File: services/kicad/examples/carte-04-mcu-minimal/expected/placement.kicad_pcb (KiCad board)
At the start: 2 copper layers, 60 x 45 mm, 15 parts, among them J1 IN_5V, J2 SWD, U1 STM32F103C8T6, U2 AMS1117-3.3

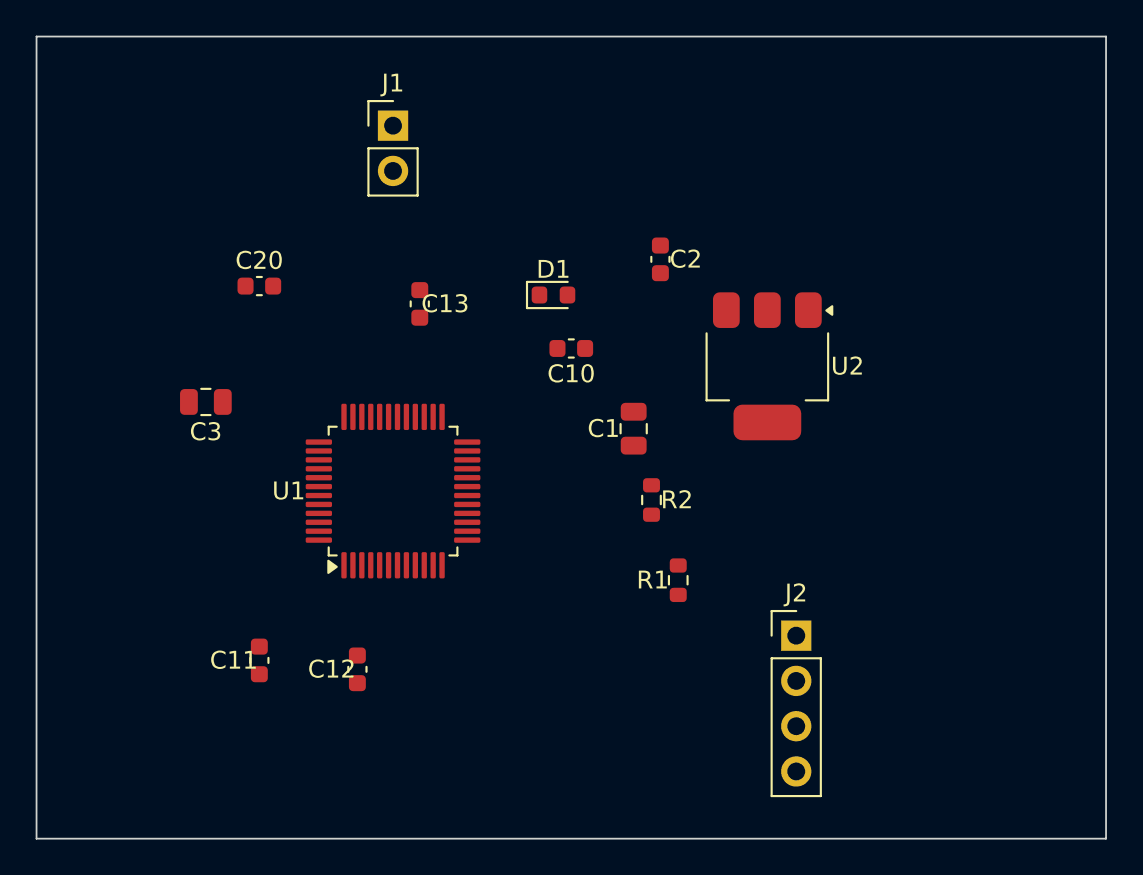
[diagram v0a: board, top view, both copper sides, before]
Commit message: examples: carte-01 a 07 -- placement valide et gele (phase 1) puis route dessus (phase 2) : 100 %, 0 erreur, 2 couches
Sequence en deux phases demandee par l'utilisateur : valider_placements.py (critere pro : chaque broche VDD a sa capa a <= 3,5 mm) puis banc_exemples.py --placement-fige. 30 s a 2,6 min de routage par carte.

Co-Authored-By: Claude Fable 5.1 <noreply@anthropic.com>

Claude-Session: https://claude.ai/code/session_01TnMqm4La2CxQHHB5K8aSSV
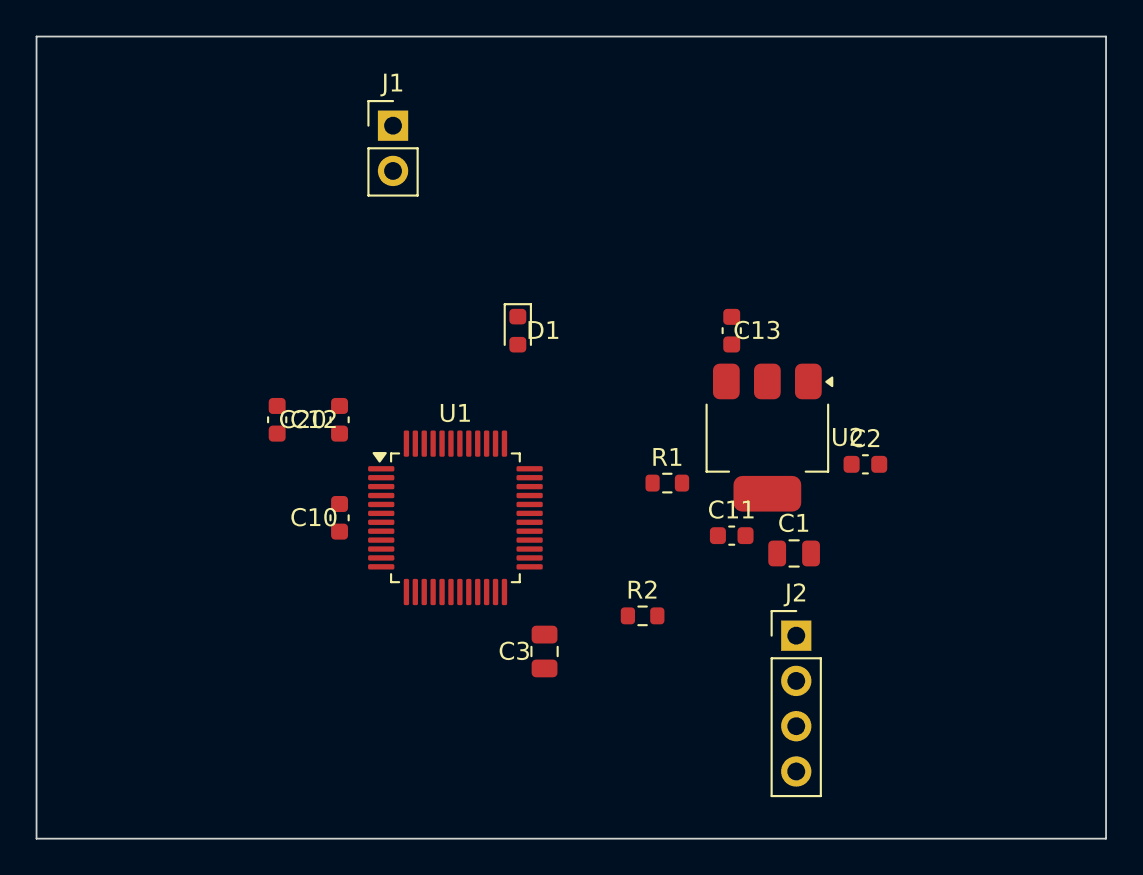
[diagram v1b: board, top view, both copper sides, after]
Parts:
- moved C11 27.4 mm to (157.5, 110.5), turned to 0 degrees
- moved C3 23.6 mm to (147.0, 117.0), turned to 90 degrees
- moved C13 17.6 mm to (157.5, 99.0)
- moved C2 16.3 mm to (165.0, 106.5), turned to 0 degrees
- moved C10 16.1 mm to (135.5, 109.5), turned to 90 degrees
- moved C12 14.0 mm to (135.5, 104.0)
- moved C1 11.4 mm to (161.0, 111.5), turned to 0 degrees
- moved C20 7.57 mm to (132.0, 104.0), turned to 270 degrees
- moved R2 6.52 mm to (152.5, 115.0), turned to 0 degrees
- moved R1 5.48 mm to (153.9, 107.6), turned to 0 degrees
- moved U2 4.00 mm to (159.5, 105.0)
- moved U1 3.81 mm to (142.0, 109.5), turned to 0 degrees
- moved D1 2.83 mm to (145.5, 99.0), turned to 270 degrees
